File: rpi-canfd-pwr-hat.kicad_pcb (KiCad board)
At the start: 4 copper layers, 65 x 56 mm, 90 parts, among them J1 Conn_01x02, J2 Conn_01x04_Pin, J3 Raspberry_Pi, J4 Conn_01x02, J5 Conn_01x02, U1 XC6206P332MR, U10 SN74LV1T125DBV, U11 SN74LV1T125DBV, U12 SN74LV1T125DBV, U13 SN74LV1T125DBV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

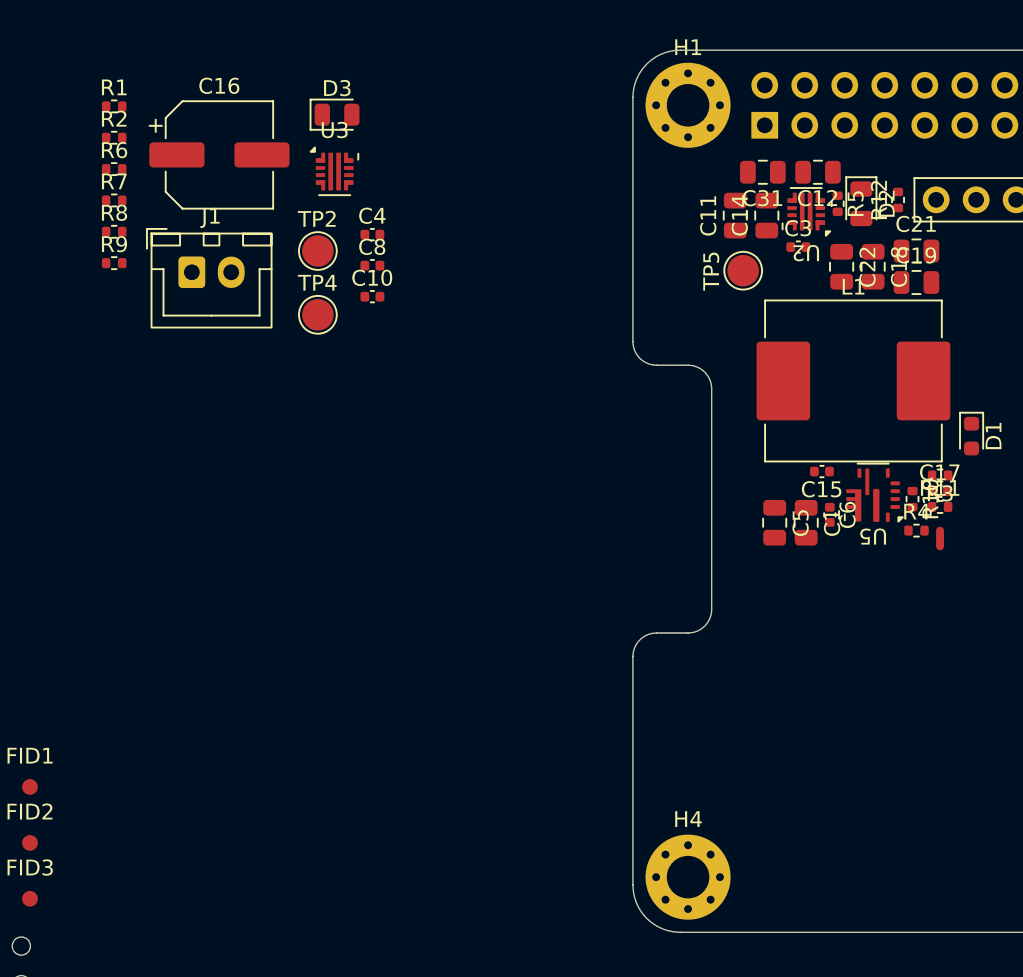
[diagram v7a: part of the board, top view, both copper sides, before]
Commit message: pcb: add input efuse routing
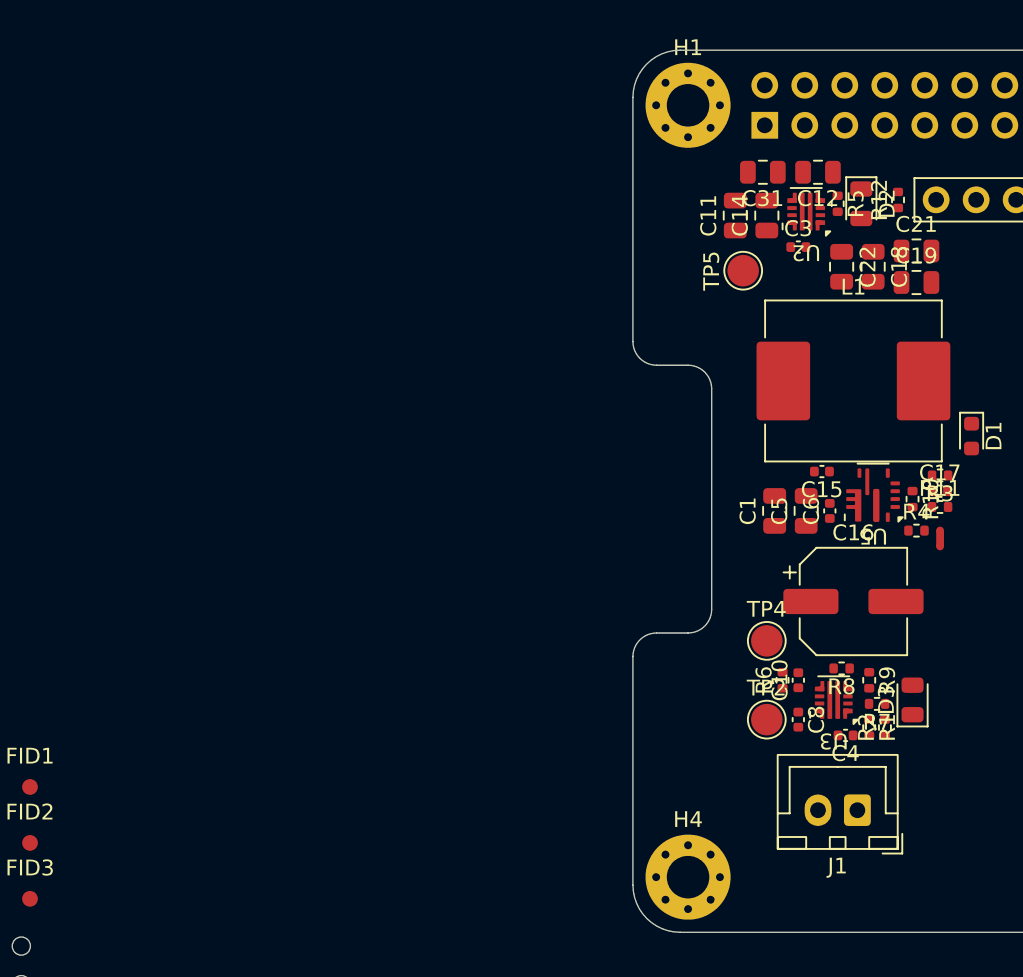
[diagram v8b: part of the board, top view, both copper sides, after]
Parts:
- moved R1 62.1 mm to (165.0, 113.0), turned to -90 degrees
- moved R2 61.6 mm to (166.0, 113.0), turned to 90 degrees
- moved R7 58.0 mm to (165.5, 111.5), turned to 180 degrees
- moved R9 54.8 mm to (165.0, 110.0), turned to -90 degrees
- moved J1 54.3 mm to (164.2, 118.2), turned to 180 degrees
- moved R8 53.9 mm to (163.2, 109.2), turned to 180 degrees
- moved R6 53.4 mm to (159.5, 110.0), turned to 90 degrees
- moved D3 52.1 mm to (167.8, 111.2), turned to 90 degrees
- moved C16 49.2 mm to (164.0, 105.0)
- moved U3 46.1 mm to (162.8, 111.2), turned to 180 degrees
- moved C4 43.7 mm to (163.5, 113.5), turned to 180 degrees
- moved TP2 41.2 mm to (158.5, 112.5)
- moved C8 39.5 mm to (160.5, 112.5), turned to -90 degrees
- moved C10 36.4 mm to (160.5, 110.0), turned to 90 degrees
- moved TP4 35.2 mm to (158.5, 107.5)
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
